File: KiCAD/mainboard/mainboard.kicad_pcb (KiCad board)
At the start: 2 copper layers, 38 parts, among them IC1 DLPC1438ZEZ, IC2 DLPA2005ERSLT, IC3 SN74AUP1G06DCKR, IC4 SN74AUP1G07DCKR, IC5 SN74AUP1G07DCKR, J1 AXT550124, J10 Conn_01x05_Pin, J30 Conn_01x08_Pin

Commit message: layout, was able to fanout all not power signals without vias inside BGA, will only need normal vias size 0.3mm diameter for GND and power planes, plan is to have DMD signals on their own layer
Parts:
- added C1: 100 uF, tp_library:CAP_EEEFT1V101AP, F.Cu at (257.5, 119.2)
- added C109: 10uF, Capacitor_SMD:C_0603_1608Metric_Pad1.08x0.95mm_HandSolder, F.Cu at (264.4, 134.8)
- added C110: 4.7uF, Capacitor_SMD:C_0603_1608Metric_Pad1.08x0.95mm_HandSolder, F.Cu at (264.4, 137.3)
- added C168: 22uF, Capacitor_SMD:C_0603_1608Metric, F.Cu at (266.5, 173.5)
- added C19: 4.7uF, Capacitor_SMD:C_0603_1608Metric_Pad1.08x0.95mm_HandSolder, F.Cu at (264.4, 122.3)
- added C2: 12pF, Capacitor_SMD:C_0603_1608Metric_Pad1.08x0.95mm_HandSolder, F.Cu at (264.4, 117.2)
- added C21: 22uF, Capacitor_SMD:C_0603_1608Metric, F.Cu at (266.5, 163.5)
- added C211: 22uF, Capacitor_SMD:C_0603_1608Metric, F.Cu at (266.5, 176.0)
- added C212: 22uF, Capacitor_SMD:C_0603_1608Metric, F.Cu at (266.5, 178.5)
- added C22: 22uF, Capacitor_SMD:C_0603_1608Metric, F.Cu at (266.5, 166.0)
- added C24: 100 uF, tp_library:CAP_EEEFT1V101AP, F.Cu at (257.5, 127.3)
- added C25: 4.7uF, Capacitor_SMD:C_0603_1608Metric_Pad1.08x0.95mm_HandSolder, F.Cu at (264.4, 124.8)
- added C26: 100nF, Capacitor_SMD:C_0603_1608Metric_Pad1.08x0.95mm_HandSolder, F.Cu at (264.4, 127.3)
- added C3: 12pF, Capacitor_SMD:C_0603_1608Metric_Pad1.08x0.95mm_HandSolder, F.Cu at (264.4, 119.8)
- added C30: 22uF, Capacitor_SMD:C_0603_1608Metric, F.Cu at (266.5, 168.5)
- added C31: 22uF, Capacitor_SMD:C_0603_1608Metric, F.Cu at (266.5, 171.0)
- added C41: 12pF, Capacitor_SMD:C_0603_1608Metric_Pad1.08x0.95mm_HandSolder, F.Cu at (264.4, 129.8)
- added C51: 100pF, Capacitor_SMD:C_0603_1608Metric_Pad1.08x0.95mm_HandSolder, F.Cu at (264.4, 132.3)
- added C71: 10 uF, Capacitor_SMD:C_0805_2012Metric_Pad1.18x1.45mm_HandSolder, F.Cu at (269.0, 117.5)
- added C72: 10 uF, Capacitor_SMD:C_0805_2012Metric_Pad1.18x1.45mm_HandSolder, F.Cu at (269.0, 120.5)
- added C73: 10 uF, Capacitor_SMD:C_0805_2012Metric_Pad1.18x1.45mm_HandSolder, F.Cu at (269.0, 123.5)
- added C74: 10 uF, Capacitor_SMD:C_0805_2012Metric_Pad1.18x1.45mm_HandSolder, F.Cu at (269.0, 126.5)
- added C82: 100 uF, tp_library:CAP_EEEFT1V101AP, F.Cu at (257.5, 135.5)
- added C96: 100 uF, tp_library:CAP_EEEFT1V101AP, F.Cu at (257.5, 143.7)
- added D10: B560C, tp_library:SMC_DIO, F.Cu at (279.9, 132.5)
- added D12: LED, LED_SMD:LED_0603_1608Metric_Pad1.05x0.95mm_HandSolder, F.Cu at (280.1, 116.5)
- added D7: SML-LX1206SIC-TR, tp_library:LED_SML-LX1206SIC-TR_LUM-M, F.Cu at (219.0, 144.3)
- added F2: 1500mA, tp_library:BLM15P_FBD-M, F.Cu at (177.1, 63.8)
- added F3: 1500mA, tp_library:BLM15P_FBD-M, F.Cu at (177.1, 66.6)
- added IC14: SN74AUP1G06DCKR, tp_library:SOT65P210X110-5N, F.Cu at (230.5, 121.2)
- added IC6: SN74AUP1G06DCKR, tp_library:SOT65P210X110-5N, F.Cu at (230.5, 117.5)
- added J10: Conn_01x05_Pin, Connector_PinHeader_2.54mm:PinHeader_1x05_P2.54mm_Vertical, F.Cu at (222.3, 130.0)
- added J100: AHDF15A-KG-TAXB, tp_library:AHDF15AKGTAXB, F.Cu at (218.9, 166.8)
- added J14: Conn_01x04_Pin, Connector_PinHeader_2.54mm:PinHeader_1x04_P2.54mm_Vertical, F.Cu at (253.0, 164.2)
- added J2: Conn_01x07_Pin, Connector_PinHeader_2.54mm:PinHeader_1x07_P2.54mm_Vertical, F.Cu at (213.1, 130.0)
- added J29: Conn_01x04_Pin, Connector_PinHeader_2.54mm:PinHeader_1x04_P2.54mm_Vertical, F.Cu at (204.3, 140.4)
- added J3: Conn_02x05_Odd_Even, Connector_PinHeader_2.54mm:PinHeader_2x05_P2.54mm_Vertical, F.Cu at (226.9, 130.0)
- added J31: Conn_01x08_Pin, Connector_PinHeader_2.54mm:PinHeader_1x08_P2.54mm_Vertical, F.Cu at (248.0, 25.9)
- added J4: Conn_01x05_Pin, Connector_PinHeader_2.54mm:PinHeader_1x05_P2.54mm_Vertical, F.Cu at (217.7, 130.0)
- added L12: LQM2HPN2R2MG0L, tp_library:IND_LQM2HPN2R2MG0L_MUR, F.Cu at (274.7, 144.5)
- added R100: 22.1k, Resistor_SMD:R_0402_1005Metric, F.Cu at (272.9, 123.0)
- added R117: 3.3k, tp_library:RES_ERJP06_PAN, F.Cu at (280.6, 120.0)
- added R155: 10k, tp_library:STA_RMCF0805_STP, F.Cu at (217.2, 120.2)
- added R156: 0, tp_library:RES_R-070RL_VIS, F.Cu at (208.7, 129.2)
- added R157: 0, tp_library:RES_R-070RL_VIS, F.Cu at (208.7, 132.2)
- added R158: 10k, tp_library:STA_RMCF0805_STP, F.Cu at (217.2, 123.2)
- added R16: 0, tp_library:RES_R-070RL_VIS, F.Cu at (197.5, 69.1)
- added R163: 10k, tp_library:STA_RMCF0805_STP, F.Cu at (217.2, 126.2)
- added R164: 10k, tp_library:STA_RMCF0805_STP, F.Cu at (221.5, 117.2)
- added R165: 10k, tp_library:STA_RMCF0805_STP, F.Cu at (221.5, 120.2)
- added R166: 10k, tp_library:STA_RMCF0805_STP, F.Cu at (221.5, 123.2)
- added R168: 100k, tp_library:RES_RMCF0805_STP, F.Cu at (225.9, 123.2)
- added R17: 100k, tp_library:RES_RMCF0805_STP, F.Cu at (232.0, 97.5)
- added R170: 10k, tp_library:STA_RMCF0805_STP, F.Cu at (221.5, 126.2)
- added R171: 0, tp_library:RES_R-070RL_VIS, F.Cu at (208.7, 135.2)
- added R174: 100k, tp_library:RES_RMCF0805_STP, F.Cu at (225.9, 126.2)
- added R19: 100k, tp_library:RES_RMCF0805_STP, F.Cu at (225.9, 120.2)
- added R212: 78.7k, Resistor_SMD:R_0402_1005Metric, F.Cu at (272.9, 124.9)
- added R213: 360k, Resistor_SMD:R_0402_1005Metric, F.Cu at (272.9, 126.9)
- added R3: 78.7k, Resistor_SMD:R_0402_1005Metric, F.Cu at (281.5, 123.0)
- added R42: 7.87k, tp_library:RES_RM10_CCE, F.Cu at (208.7, 123.2)
- added R5: 100, tp_library:RES_CRCW_0805, F.Cu at (217.5, 147.7)
- added R52: 7.87k, tp_library:RES_RM10_CCE, F.Cu at (208.7, 126.2)
- added R53: 3.3k, tp_library:RES_ERJP06_PAN, F.Cu at (212.9, 117.2)
- added R54: 3.3k, tp_library:RES_ERJP06_PAN, F.Cu at (212.9, 120.2)
- added R55: 3.3k, tp_library:RES_ERJP06_PAN, F.Cu at (212.6, 123.6)
- added R7: 100, tp_library:RES_CRCW_0805, F.Cu at (217.5, 150.8)
- added R73: 3.3k, tp_library:RES_ERJP06_PAN, F.Cu at (212.9, 126.2)
- added R8: 0, tp_library:RES_R-070RL_VIS, F.Cu at (208.7, 117.2)
- added R84: 10k, tp_library:STA_RMCF0805_STP, F.Cu at (259.6, 166.5)
- added R92: 10k, tp_library:STA_RMCF0805_STP, F.Cu at (217.2, 117.2)
- added R95: 22.1k, Resistor_SMD:R_0402_1005Metric, F.Cu at (282.0, 126.0)
- added R99: 22.1k, Resistor_SMD:R_0402_1005Metric, F.Cu at (272.9, 121.0)
- added TP12: TestPoint, TestPoint:TestPoint_Pad_D1.5mm, F.Cu at (233.5, 133.0)
- added TP20: TestPoint, TestPoint:TestPoint_Pad_D1.5mm, F.Cu at (233.5, 136.6)
- added TP21: TestPoint, TestPoint:TestPoint_Pad_D1.5mm, F.Cu at (233.5, 140.1)
- added TP7: TestPoint, TestPoint:TestPoint_Pad_D1.5mm, F.Cu at (233.5, 129.5)
- added U12: ECS-2520MV-xxx-xx, Oscillator:Oscillator_SMD_ECS_2520MV-xxx-xx-4Pin_2.5x2.0mm, F.Cu at (196.8, 58.6)
- added U13: MX25L3233FM2, Package_SO:SOIC-8_5.3x5.3mm_P1.27mm, F.Cu at (229.7, 146.0)
- added U22: TXS0102DCU, Package_SO:VSSOP-8_2.3x2mm_P0.5mm, F.Cu at (232.0, 102.5)
- added U26: TPS54340DDA, Package_SO:TI_SO-PowerPAD-8_ThermalVias, F.Cu at (270.9, 139.3)
- added U37: TXS0102DCU, Package_SO:VSSOP-8_2.3x2mm_P0.5mm, F.Cu at (232.0, 108.0)
- added U39: TPS62260DDCT, tp_library:DDC5, F.Cu at (269.4, 144.9)
- added U7: SN74AUP1G06DCKR, tp_library:SOT65P210X110-5N, F.Cu at (230.5, 124.9)
- C169: renamed from C22; value 22u -> 22uF
- R15, R197: footprint Resistor_SMD:R_0402_1005Metric -> tp_library:STA_RMCF0805_STP
- R176, R177, R178, R179: footprint Resistor_SMD:R_0402_1005Metric -> tp_library:RES_RMCF0805_STP
- moved REF** 208.1 mm to (59.5, 229.0)
- moved REF** 208.1 mm to (49.0, 234.5)
- moved REF** 208.1 mm to (24.0, 237.5)
- moved REF** 208.1 mm to (85.5, 235.5)
- moved REF** 208.1 mm to (24.5, 229.5)
- moved REF** 208.1 mm to (48.5, 229.0)
- moved REF** 208.1 mm to (69.5, 244.0)
- moved REF** 208.1 mm to (50.0, 239.5)
- moved REF** 208.1 mm to (69.5, 234.5)
- moved REF** 197.9 mm to (35.8, 222.0)
- moved U16 53.3 mm to (206.8, 59.0)
- moved J1 27.3 mm to (94.9, 52.2)
- moved U24 27.3 mm to (149.8, 51.5)
- moved C116 12.7 mm to (138.5, 94.5)
- moved C117 12.7 mm to (138.5, 96.5)
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- renumbered IC1 to U16, IC2 to U24
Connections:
- net GPIO_12 renamed /DLPC1438_Interface/GPIO_12
- net GPIO_15 renamed /DLPC1438_Interface/GPIO_15
- net GPIO_16 renamed /DLPC1438_Interface/GPIO_16
- net GPIO_17 renamed /DLPC1438_Interface/GPIO_17
- net GPIO_18 renamed /DLPC1438_Interface/GPIO_18
- net GPIO_19 renamed /DLPC1438_Interface/GPIO_19
- net GPIO_4 renamed /DLPC1438_Interface/GPIO_4
- net GPIO_5 renamed /DLPC1438_Interface/GPIO_5
- C116 pad 1: P1P8V_DLPC -> GND
- C116 pad 2: GND -> P1P8V_DLPC
- C122 pad 1: /DMD_Interface/VOFS -> GND
- C122 pad 2: GND -> /DMD_Interface/VOFS
- C123 pad 1: /DMD_Interface/VBIAS -> GND
- C123 pad 2: GND -> /DMD_Interface/VBIAS
- C124 pad 1: /DMD_Interface/VRST -> GND
- C124 pad 2: GND -> /DMD_Interface/VRST
- C13 pad 1: /DMD_Interface/VRST -> GND
- C13 pad 2: GND -> /DMD_Interface/VRST
- C14 pad 1: /DMD_Interface/VBIAS -> GND
- C14 pad 2: GND -> /DMD_Interface/VBIAS
- C15 pad 1: /DMD_Interface/VOFS -> GND
- C15 pad 2: GND -> /DMD_Interface/VOFS
- C169 pad 1: unconnected-(C22-Pad1) -> P5V
- C169 pad 2: unconnected-(C22-Pad2) -> GND
- R15 pad 1: P3V3V -> /DMD_Interface/SYS_RDY
- R15 pad 2: /DMD_Interface/SYS_RDY -> P3V3V
- R176 pad 1: SPI1_CLK -> /DLPC1438_Interface/SPI1_CLK
- R177 pad 1: SPI1_CSZ0 -> P1P8V_DLPC
- R177 pad 2: P1P8V_DLPC -> /DLPC1438_Interface/GPIO_3
- R178 pad 1: GND -> /DLPC1438_Interface/SPI1_MOSI
- R178 pad 2: SPI1_MOSI -> GND
- R179 pad 1: GND -> /DLPC1438_Interface/SPI1_MISO
- R179 pad 2: SPI1_MISO -> GND
- R197 pad 1: P3V3V -> /DMD_Interface/PRINT_ACTIVE
- R197 pad 2: /DMD_Interface/PRINT_ACTIVE -> P3V3V
- U16 pad A12: unconnected-(IC1-CMP_OUT-PadA12) -> /DLPC1438_Interface/CMP_OUT
- U16 pad A13: unconnected-(IC1-SPI0_CLK-PadA13) -> /DLPC1438_Interface/DLPC_SPICLK
- U16 pad A14: unconnected-(IC1-SPI0_CSZ0-PadA14) -> /DLPC1438_Interface/DLPC_SPICSZ0
- U16 pad B12: unconnected-(IC1-SPI0_DIN-PadB12) -> /DLPC1438_Interface/SPI0_MISO
- U16 pad B13: unconnected-(IC1-SPI0_DOUT-PadB13) -> /DLPC1438_Interface/DLPC_SPIDOUT
- U16 pad B14: unconnected-(IC1-LED_SEL_1-PadB14) -> /DLPC1438_Interface/DLPC_LED_SEL_1
- U16 pad B15: unconnected-(IC1-LED_SEL_0-PadB15) -> /DLPC1438_Interface/DLPC_LED_SEL_0
- U16 pad C10: unconnected-(IC1-HWTEST_E_N-PadC10) -> GND
- U16 pad C11: unconnected-(IC1-RESETZ-PadC11) -> /DLPC1438_Interface/RESETZ
- U16 pad C13: unconnected-(IC1-PARKZ-PadC13) -> /DLPC1438_Interface/INTZ
- U16 pad C14: SPI1_MISO -> /DLPC1438_Interface/SPI1_MISO
- U16 pad C3: unconnected-(IC1-VDDLP12-PadC3) -> P1P1V
- U16 pad C4: unconnected-(IC1-VSS_1-PadC4) -> GND
- U16 pad C5: unconnected-(IC1-VDD_1-PadC5) -> P1P1V
- U16 pad C6: unconnected-(IC1-VSS_2-PadC6) -> GND
- U16 pad C7: unconnected-(IC1-VCC_1-PadC7) -> /DLPC1438_Interface/VCC
- U16 pad C8: unconnected-(IC1-VSS_3-PadC8) -> GND
- U16 pad C9: unconnected-(IC1-VCC_2-PadC9) -> /DLPC1438_Interface/VCC
- U16 pad D10: unconnected-(IC1-VSS_6-PadD10) -> GND
- U16 pad D11: unconnected-(IC1-VCC_FLSH-PadD11) -> P3P3V_SB
- U16 pad D12: unconnected-(IC1-VDD_6-PadD12) -> P1P1V
- U16 pad D13: unconnected-(IC1-VDD_7-PadD13) -> P1P1V
- U16 pad D3: unconnected-(IC1-VDD_2-PadD3) -> P1P1V
- U16 pad D4: unconnected-(IC1-VCC_3-PadD4) -> P1P8V_DLPC
- U16 pad D5: unconnected-(IC1-VDD_3-PadD5) -> P1P1V
- U16 pad D6: unconnected-(IC1-VSS_4-PadD6) -> GND
- U16 pad D7: unconnected-(IC1-VDD_4-PadD7) -> P1P1V
- U16 pad D8: unconnected-(IC1-VSS_5-PadD8) -> GND
- U16 pad D9: unconnected-(IC1-VDD_5-PadD9) -> P1P1V
- U16 pad E12: unconnected-(IC1-VCC_4-PadE12) -> P1P8V_DLPC
- U16 pad E13: unconnected-(IC1-VSS_8-PadE13) -> GND
- U16 pad E3: unconnected-(IC1-VDD_8-PadE3) -> P1P1V
- U16 pad E4: unconnected-(IC1-VSS_7-PadE4) -> GND
- U16 pad F10: unconnected-(IC1-VSS_14-PadF10) -> Net-(U16-VSS_10)
- U16 pad F12: unconnected-(IC1-VCC_5-PadF12) -> P1P8V_DLPC
- U16 pad F13: unconnected-(IC1-VDD_9-PadF13) -> P1P1V
- U16 pad F4: unconnected-(IC1-VSS_9-PadF4) -> GND
- U16 pad F6: unconnected-(IC1-VSS_10-PadF6) -> Net-(U16-VSS_10)
- U16 pad F7: unconnected-(IC1-VSS_11-PadF7) -> Net-(U16-VSS_10)
- U16 pad F8: unconnected-(IC1-VSS_12-PadF8) -> Net-(U16-VSS_10)
- U16 pad F9: unconnected-(IC1-VSS_13-PadF9) -> Net-(U16-VSS_10)
- U16 pad G10: unconnected-(IC1-VSS_20-PadG10) -> GND
- U16 pad G12: unconnected-(IC1-VSS_21-PadG12) -> GND
- U16 pad G13: unconnected-(IC1-VSS_22-PadG13) -> GND
- U16 pad G14: /DLPC1438_Interface/PROJ_ON -> /DLPA2005_Interface/PROJ_ON
- U16 pad G3: unconnected-(IC1-VSS_PLLM-PadG3) -> /DLPC1438_Interface/VSS_PLL
- U16 pad G4: unconnected-(IC1-VSS_15-PadG4) -> GND
- U16 pad G6: unconnected-(IC1-VSS_16-PadG6) -> GND
- U16 pad G7: unconnected-(IC1-VSS_17-PadG7) -> GND
- U16 pad G8: unconnected-(IC1-VSS_18-PadG8) -> GND
- U16 pad G9: unconnected-(IC1-VSS_19-PadG9) -> GND
- U16 pad H1: unconnected-(IC1-PLL_REFCL_K_I-PadH1) -> /DLPC1438_Interface/OSC_OUT
- U16 pad H10: unconnected-(IC1-VSS_28-PadH10) -> GND
- U16 pad H12: unconnected-(IC1-VSS_29-PadH12) -> GND
- U16 pad H13: unconnected-(IC1-VDD_10-PadH13) -> P1P1V
- U16 pad H14: /DLPC1438_Interface/RC_CHARGE -> /DLPA2005_Interface/RC_CHARGE
- U16 pad H2: unconnected-(IC1-VDD_PLLM-PadH2) -> /DLPC1438_Interface/VDD_PLL
- U16 pad H3: unconnected-(IC1-VSS_PLLD-PadH3) -> /DLPC1438_Interface/VSS_PLL
- U16 pad H4: unconnected-(IC1-VSS_23-PadH4) -> GND
- U16 pad H6: unconnected-(IC1-VSS_24-PadH6) -> GND
- U16 pad H7: unconnected-(IC1-VSS_25-PadH7) -> GND
- U16 pad H8: unconnected-(IC1-VSS_26-PadH8) -> GND
- U16 pad H9: unconnected-(IC1-VSS_27-PadH9) -> GND
- U16 pad J1: unconnected-(IC1-PLL_REFCL_K_O-PadJ1) -> /DLPC1438_Interface/DLPC_PLLO
- U16 pad J10: unconnected-(IC1-VSS_35-PadJ10) -> GND
- U16 pad J12: unconnected-(IC1-VDD_12-PadJ12) -> P1P1V
- U16 pad J13: unconnected-(IC1-VSS_36-PadJ13) -> GND
- U16 pad J2: unconnected-(IC1-VDD_PLLD-PadJ2) -> /DLPC1438_Interface/VDD_PLL
- U16 pad J3: unconnected-(IC1-VSS_30-PadJ3) -> GND
- U16 pad J4: unconnected-(IC1-VDD_11-PadJ4) -> P1P1V
- U16 pad J6: unconnected-(IC1-VSS_31-PadJ6) -> GND
- U16 pad J7: unconnected-(IC1-VSS_32-PadJ7) -> GND
- U16 pad J8: unconnected-(IC1-VSS_33-PadJ8) -> GND
- U16 pad J9: unconnected-(IC1-VSS_34-PadJ9) -> GND
- U16 pad K1: unconnected-(IC1-PDATA_1-PadK1) -> /DLPC1438_Interface/PDATA1
- U16 pad K10: unconnected-(IC1-VSS_42-PadK10) -> GND
- U16 pad K12: unconnected-(IC1-VSS_43-PadK12) -> GND
- U16 pad K13: unconnected-(IC1-VCC_6-PadK13) -> P1P8V_DLPC
- U16 pad K2: unconnected-(IC1-PDATA_0-PadK2) -> /DLPC1438_Interface/PDATA0
- U16 pad K3: unconnected-(IC1-VDD_13-PadK3) -> P1P1V
- U16 pad K4: unconnected-(IC1-VSS_37-PadK4) -> GND
- U16 pad K6: unconnected-(IC1-VSS_38-PadK6) -> GND
- U16 pad K7: unconnected-(IC1-VSS_39-PadK7) -> GND
- U16 pad K8: unconnected-(IC1-VSS_40-PadK8) -> GND
- U16 pad K9: unconnected-(IC1-VSS_41-PadK9) -> GND
- U16 pad L1: unconnected-(IC1-PDATA_3-PadL1) -> /DLPC1438_Interface/PDATA3
- U16 pad L12: unconnected-(IC1-VDD_15-PadL12) -> P1P1V
- U16 pad L13: unconnected-(IC1-VDD_16-PadL13) -> P1P1V
- U16 pad L2: unconnected-(IC1-PDATA_2-PadL2) -> /DLPC1438_Interface/PDATA2
- U16 pad L3: unconnected-(IC1-VSS_44-PadL3) -> GND
- U16 pad L4: unconnected-(IC1-VDD_14-PadL4) -> P1P1V
- U16 pad M1: unconnected-(IC1-PDATA_5-PadM1) -> /DLPC1438_Interface/PDATA5
- U16 pad M10: unconnected-(IC1-VDD_19-PadM10) -> P1P1V
- U16 pad M11: unconnected-(IC1-VCC_7-PadM11) -> P1P8V_DLPC
- U16 pad M12: unconnected-(IC1-VSS_48-PadM12) -> GND
- U16 pad M13: unconnected-(IC1-JTAGTMS1-PadM13) -> /DLPC1438_Interface/JTAG_TMS
- U16 pad M2: unconnected-(IC1-PDATA_4-PadM2) -> /DLPC1438_Interface/PDATA4
- U16 pad M3: unconnected-(IC1-VCC_INTF_1-PadM3) -> P1P8V_DLPC
- U16 pad M4: unconnected-(IC1-VSS_45-PadM4) -> GND
- U16 pad M5: unconnected-(IC1-VSS_46-PadM5) -> GND
- U16 pad M6: unconnected-(IC1-VDD_17-PadM6) -> P1P1V
- U16 pad M7: unconnected-(IC1-VCC_INTF_2-PadM7) -> P1P8V_DLPC
- U16 pad M8: unconnected-(IC1-VSS_47-PadM8) -> GND
- U16 pad M9: unconnected-(IC1-VDD_18-PadM9) -> P1P1V
- U16 pad N1: unconnected-(IC1-PDATA_7-PadN1) -> /DLPC1438_Interface/PDATA7
- U16 pad N10: unconnected-(IC1-IIC0_SCL-PadN10) -> /DLPC1438_Interface/IIC0_SCL
- U16 pad N13: unconnected-(IC1-JTAGTDO1-PadN13) -> /DLPC1438_Interface/JTAG_TDO
- U16 pad N14: unconnected-(IC1-TSTPT_6-PadN14) -> /DLPC1438_Interface/TSTPT_6
- U16 pad N15: unconnected-(IC1-TSTPT_7-PadN15) -> /DLPC1438_Interface/TSTPT_7
- U16 pad N2: unconnected-(IC1-PDATA_6-PadN2) -> /DLPC1438_Interface/PDATA6
- U16 pad N3: unconnected-(IC1-VCC_INTF_3-PadN3) -> P1P8V_DLPC
- U16 pad N4: unconnected-(IC1-PDM_CVS__TE-PadN4) -> /DLPC1438_Interface/PDM_CVS_TE
- U16 pad N5: unconnected-(IC1-HSYNC_CS-PadN5) -> /DLPC1438_Interface/HSYNC
- U16 pad N6: unconnected-(IC1-3DR-PadN6) -> /DLPC1438_Interface/DLPC_3DR
- U16 pad N7: unconnected-(IC1-VCC_INTF_4-PadN7) -> P1P8V_DLPC
- U16 pad N8: unconnected-(IC1-HOST_IRQ-PadN8) -> /DLPC1438_Interface/DLPC_HOST_IRQ
- U16 pad N9: unconnected-(IC1-IIC0_SDA-PadN9) -> /DLPC1438_Interface/IIC0_SDA
- U16 pad P1: unconnected-(IC1-VSYNC_WE-PadP1) -> /DLPC1438_Interface/VSYNC
- U16 pad P10: unconnected-(IC1-PDATA_23-PadP10) -> GND
- U16 pad P11: unconnected-(IC1-JTAGTRSTZ-PadP11) -> /DLPC1438_Interface/JTAG_TRSTZ
- U16 pad P12: unconnected-(IC1-JTAGTCK-PadP12) -> /DLPC1438_Interface/JTAG_TCK
- U16 pad P13: unconnected-(IC1-JTAGTDI-PadP13) -> /DLPC1438_Interface/JTAG_TDI
- U16 pad P14: unconnected-(IC1-TSTPT_4-PadP14) -> /DLPC1438_Interface/TSTPT_4
- U16 pad P15: unconnected-(IC1-TSTPT_5-PadP15) -> /DLPC1438_Interface/TSTPT_5
- U16 pad P2: unconnected-(IC1-DATEN_CM_D-PadP2) -> /DLPC1438_Interface/DATEN_CM_D
- U16 pad P3: unconnected-(IC1-PCLK-PadP3) -> /DLPC1438_Interface/PCLK
- U16 pad P4: unconnected-(IC1-PDATA_11-PadP4) -> GND
- U16 pad P5: unconnected-(IC1-PDATA_13-PadP5) -> GND
- U16 pad P6: unconnected-(IC1-PDATA_15-PadP6) -> GND
- U16 pad P7: unconnected-(IC1-PDATA_17-PadP7) -> GND
- U16 pad P8: unconnected-(IC1-PDATA_19-PadP8) -> GND
- U16 pad P9: unconnected-(IC1-PDATA_21-PadP9) -> GND
- U16 pad R1: unconnected-(IC1-PDATA_8-PadR1) -> GND
- U16 pad R10: unconnected-(IC1-IIC1_SDA-PadR10) -> /DLPC1438_Interface/IIC1_SCL
- U16 pad R11: unconnected-(IC1-IIC1_SCL-PadR11) -> /DLPC1438_Interface/IIC1_SDA
- U16 pad R12: unconnected-(IC1-TSTPT_0-PadR12) -> /DLPC1438_Interface/TSTPT_0
- U16 pad R13: unconnected-(IC1-TSTPT_1-PadR13) -> /DLPC1438_Interface/TSTPT_1
- U16 pad R14: unconnected-(IC1-TSTPT_2-PadR14) -> /DLPC1438_Interface/TSTPT_2
- U16 pad R15: unconnected-(IC1-TSTPT_3-PadR15) -> /DLPC1438_Interface/TSTPT_3
- U16 pad R2: unconnected-(IC1-PDATA_9-PadR2) -> GND
- U16 pad R3: unconnected-(IC1-PDATA_10-PadR3) -> GND
- U16 pad R4: unconnected-(IC1-PDATA_12-PadR4) -> GND
- U16 pad R5: unconnected-(IC1-PDATA_14-PadR5) -> GND
- U16 pad R6: unconnected-(IC1-PDATA_16-PadR6) -> GND
- U16 pad R7: unconnected-(IC1-PDATA_18-PadR7) -> GND
- U16 pad R8: unconnected-(IC1-PDATA_20-PadR8) -> GND
- U16 pad R9: unconnected-(IC1-PDATA_22-PadR9) -> GND
- U24 pad 1: unconnected-(IC2-VINL_1-Pad1) -> P5V
- U24 pad 10: unconnected-(IC2-VINR-Pad10) -> P5V
- U24 pad 11: unconnected-(IC2-SWN-Pad11) -> Net-(D18-K)
- U24 pad 12: unconnected-(IC2-PGNDR-Pad12) -> GND
- U24 pad 13: unconnected-(IC2-SWP-Pad13) -> Net-(U24-SWP)
- U24 pad 14: unconnected-(IC2-CNTR_VRST-Pad14) -> VRST
- U24 pad 15: unconnected-(IC2-VBIAS-Pad15) -> VBIAS
- U24 pad 17: unconnected-(IC2-VOFS-Pad17) -> VOFS
- U24 pad 18: unconnected-(IC2-VINA-Pad18) -> P5V
- U24 pad 19: unconnected-(IC2-V2V5-Pad19) -> V2V5
- U24 pad 2: unconnected-(IC2-VINL_2-Pad2) -> P5V
- U24 pad 20: unconnected-(IC2-GND-Pad20) -> GND
- U24 pad 21: unconnected-(IC2-LS_OUT-Pad21) -> Net-(U24-LS_OUT)
- U24 pad 22: unconnected-(IC2-LS_IN-Pad22) -> P1P8V
- U24 pad 23: unconnected-(IC2-PGNDC-Pad23) -> GND
- U24 pad 24: unconnected-(IC2-SWC-Pad24) -> Net-(U24-SWC)
- U24 pad 25: unconnected-(IC2-VINC-Pad25) -> P5V
- U24 pad 26: unconnected-(IC2-PWM_IN-Pad26) -> /DLPA2005_Interface/RC_CHARGE
- U24 pad 27: unconnected-(IC2-PROJ_ON-Pad27) -> /DLPA2005_Interface/PROJ_ON
- U24 pad 28: unconnected-(IC2-CMP_OUT-Pad28) -> /DLPC1438_Interface/CMP_OUT
- U24 pad 29: unconnected-(IC2-VCORE-Pad29) -> P1P1V
- U24 pad 3: unconnected-(IC2-SPI_DIN-Pad3) -> /DLPC1438_Interface/SPI1_MOSI
- U24 pad 30: unconnected-(IC2-SENS2-Pad30) -> Net-(U24-SENS2)
- U24 pad 31: unconnected-(IC2-LED_SEL0-Pad31) -> Net-(U24-LED_SEL0)
- U24 pad 32: unconnected-(IC2-VSPI-Pad32) -> P1P8V_DLPC
- U24 pad 33: unconnected-(IC2-SENS1-Pad33) -> Net-(U24-SENS1)
- U24 pad 34: unconnected-(IC2-LED_SEL1-Pad34) -> /DLPA2005_Interface/LED_SEL_1
- U24 pad 35: unconnected-(IC2-V6V-Pad35) -> V6V
- U24 pad 36: unconnected-(IC2-RLIM_K-Pad36) -> Net-(U24-RLIM)
- U24 pad 38: unconnected-(IC2-SW5-Pad38) -> /DLPA2005_Interface/GRN_CATHODE
- U24 pad 4: /DLPA2005_Interface/RESETZ -> /DLPC1438_Interface/RESETZ
- U24 pad 40: unconnected-(IC2-RLIM-Pad40) -> Net-(U24-RLIM)
- U24 pad 41: unconnected-(IC2-VLED_1-Pad41) -> /DLPA2005_Interface/LED_ANODE
- U24 pad 42: unconnected-(IC2-VLED_2-Pad42) -> /DLPA2005_Interface/LED_ANODE
- U24 pad 43: unconnected-(IC2-L2_1-Pad43) -> Net-(U24-L2_1)
- U24 pad 44: unconnected-(IC2-L2_2-Pad44) -> Net-(U24-L2_1)
- U24 pad 45: unconnected-(IC2-PGNDL_1-Pad45) -> GND
- U24 pad 46: unconnected-(IC2-PGNDL_2-Pad46) -> GND
- U24 pad 47: unconnected-(IC2-L1_1-Pad47) -> Net-(U24-L1_1)
- U24 pad 48: unconnected-(IC2-L1_2-Pad48) -> Net-(U24-L1_1)
- U24 pad 49: unconnected-(IC2-EP-Pad49) -> GND
- U24 pad 5: unconnected-(IC2-AGND1-Pad5) -> GND
- U24 pad 6: unconnected-(IC2-INTZ-Pad6) -> /DLPC1438_Interface/INTZ
- U24 pad 7: unconnected-(IC2-SPI_CLK-Pad7) -> /DLPC1438_Interface/SPI1_CLK
- U24 pad 8: unconnected-(IC2-SPI_CSZ-Pad8) -> /DLPC1438_Interface/SPI1_CSZ0
- U24 pad 9: unconnected-(IC2-SPI_DOUT-Pad9) -> Net-(U24-SPI_DOUT)
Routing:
- net /DLPC1438_Interface/RESETZ: track 0.00 -> 9.64 mm
- net P1P1V: track 0.00 -> 9.31 mm
- net /DLPC1438_Interface/VSS_PLL: track 0.00 -> 6.40 mm
- net P1P8V_DLPC: track 0.00 -> 5.98 mm
- net /DLPC1438_Interface/VDD_PLL: track 0.00 -> 5.42 mm
- net /DLPC1438_Interface/INTZ: track 0.00 -> 4.11 mm
- net /DLPC1438_Interface/DMD_HS_WDATAC_N: track 0.00 -> 3.52 mm
- net /DLPC1438_Interface/SPI0_MISO: track 0.00 -> 3.44 mm
- net /DLPC1438_Interface/JTAG_TMS: track 0.00 -> 3.44 mm
- net /DLPC1438_Interface/JTAG_TDO: track 0.00 -> 3.43 mm
- net /DLPC1438_Interface/DLPC_SPIDOUT: track 0.00 -> 3.42 mm
- net /DLPC1438_Interface/IIC0_SCL: track 0.00 -> 3.35 mm
- net /DLPC1438_Interface/DMD_HS_WDATAB_N: track 0.00 -> 3.35 mm
- net /DLPC1438_Interface/DMD_HS_WDATAA_N: track 0.00 -> 3.28 mm
- net /DLPC1438_Interface/DLPC_LED_SEL_1: track 0.00 -> 3.21 mm
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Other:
- copper layers 2 -> 10

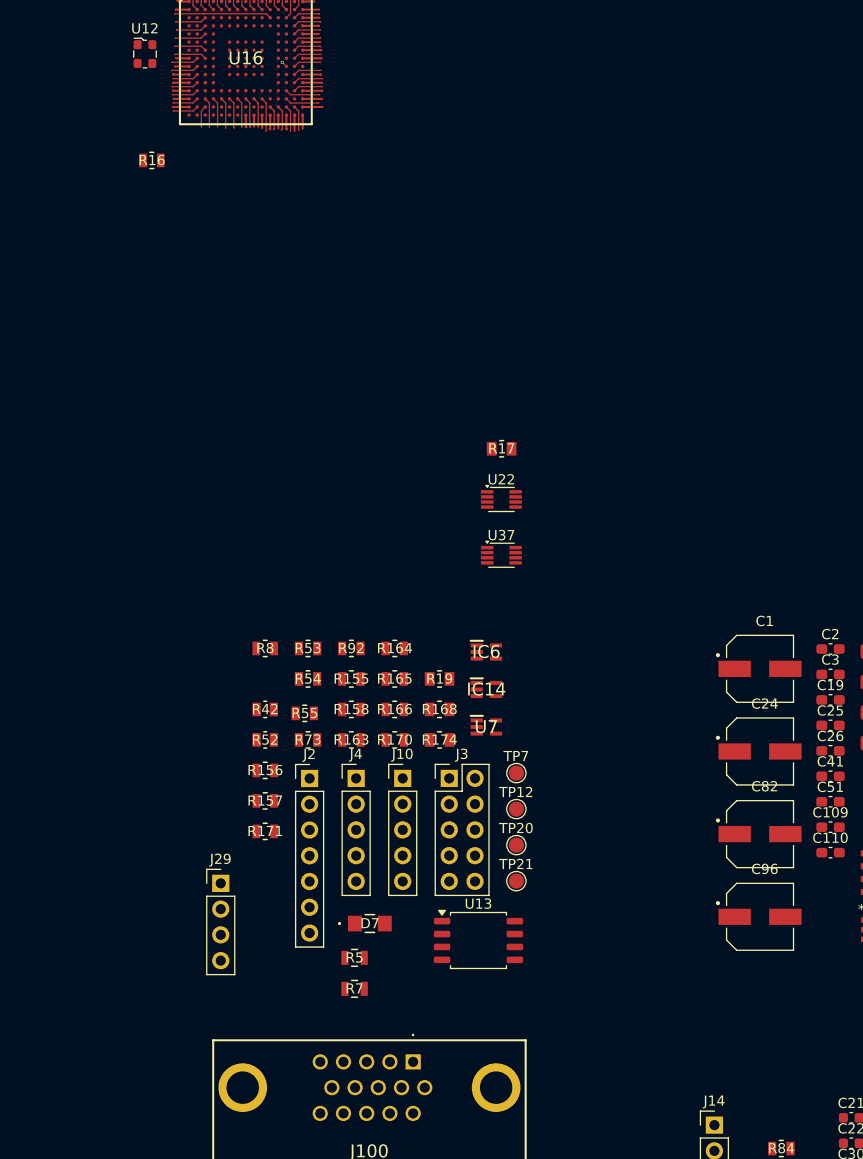
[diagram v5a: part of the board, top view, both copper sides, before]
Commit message: added pours to pcb and fixed DLPC capacitor errors
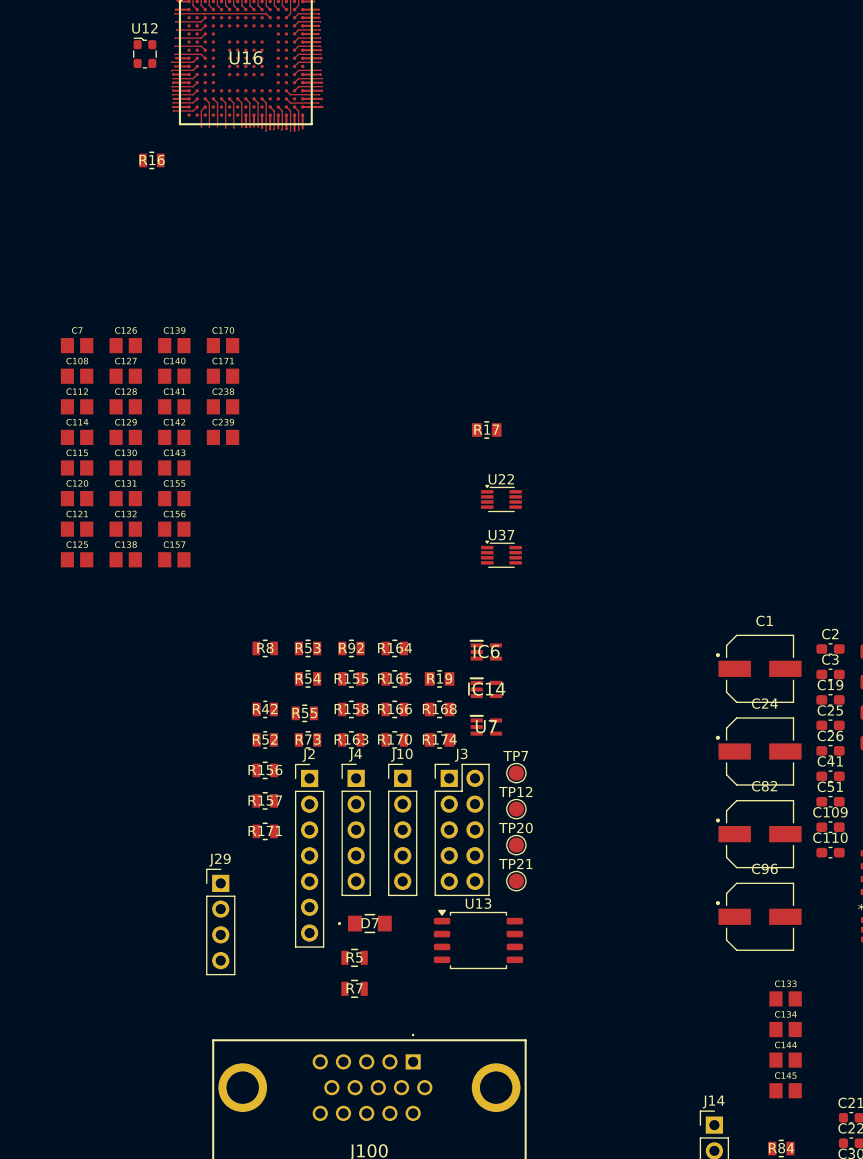
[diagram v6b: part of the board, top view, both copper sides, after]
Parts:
- added C108: 100n, tp_library:CAPC2012X70, F.Cu at (190.2, 90.3)
- added C112: 100n, tp_library:CAPC2012X70, F.Cu at (190.2, 93.4)
- added C114: 100n, tp_library:CAPC2012X70, F.Cu at (190.2, 96.4)
- added C115: 100n, tp_library:CAPC2012X70, F.Cu at (190.2, 99.4)
- added C120: 100n, tp_library:CAPC2012X70, F.Cu at (190.2, 102.4)
- added C121: 100n, tp_library:CAPC2012X70, F.Cu at (190.2, 105.4)
- added C125: 100n, tp_library:CAPC2012X70, F.Cu at (190.2, 108.4)
- added C126: 100n, tp_library:CAPC2012X70, F.Cu at (195.0, 87.3)
- added C127: 100n, tp_library:CAPC2012X70, F.Cu at (195.0, 90.3)
- added C128: 100n, tp_library:CAPC2012X70, F.Cu at (195.0, 93.4)
- added C129: 100n, tp_library:CAPC2012X70, F.Cu at (195.0, 96.4)
- added C130: 100n, tp_library:CAPC2012X70, F.Cu at (195.0, 99.4)
- added C131: 100n, tp_library:CAPC2012X70, F.Cu at (195.0, 102.4)
- added C132: 100n, tp_library:CAPC2012X70, F.Cu at (195.0, 105.4)
- added C133: 100n, tp_library:CAPC2012X70, F.Cu at (260.0, 151.7)
- added C134: 100n, tp_library:CAPC2012X70, F.Cu at (260.0, 154.8)
- added C138: 100n, tp_library:CAPC2012X70, F.Cu at (195.0, 108.4)
- added C139: 100n, tp_library:CAPC2012X70, F.Cu at (199.8, 87.3)
- added C140: 100n, tp_library:CAPC2012X70, F.Cu at (199.8, 90.3)
- added C141: 100n, tp_library:CAPC2012X70, F.Cu at (199.8, 93.4)
- added C142: 100n, tp_library:CAPC2012X70, F.Cu at (199.8, 96.4)
- added C143: 100n, tp_library:CAPC2012X70, F.Cu at (199.8, 99.4)
- added C144: 100n, tp_library:CAPC2012X70, F.Cu at (260.0, 157.8)
- added C145: 100n, tp_library:CAPC2012X70, F.Cu at (260.0, 160.8)
- added C155: 100n, tp_library:CAPC2012X70, F.Cu at (199.8, 102.4)
- added C156: 100n, tp_library:CAPC2012X70, F.Cu at (199.8, 105.4)
- added C157: 100n, tp_library:CAPC2012X70, F.Cu at (199.8, 108.4)
- added C170: 100n, tp_library:CAPC2012X70, F.Cu at (204.5, 87.3)
- added C171: 100n, tp_library:CAPC2012X70, F.Cu at (204.5, 90.3)
- added C238: 100n, tp_library:CAPC2012X70, F.Cu at (204.5, 93.4)
- added C239: 100n, tp_library:CAPC2012X70, F.Cu at (204.5, 96.4)
- added C7: 100n, tp_library:CAPC2012X70, F.Cu at (190.2, 87.3)
- moved R17 2.36 mm to (230.6, 95.7)
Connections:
- U16 pad F10: Net-(U16-VSS_10) -> GND
- U16 pad F6: Net-(U16-VSS_10) -> GND
- U16 pad F7: Net-(U16-VSS_10) -> GND
- U16 pad F8: Net-(U16-VSS_10) -> GND
- U16 pad F9: Net-(U16-VSS_10) -> GND
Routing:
- net GND: track 2.95 -> 2.36 mm, vias 1 -> 0
- added copper zone on In1.Cu, net GND
- added copper zone on In8.Cu, net GND
- added copper zone on In3.Cu, net P1P1V
- added copper zone on In6.Cu, net P1P8V_DLPC
- added copper zone on In5.Cu, net P3P3V

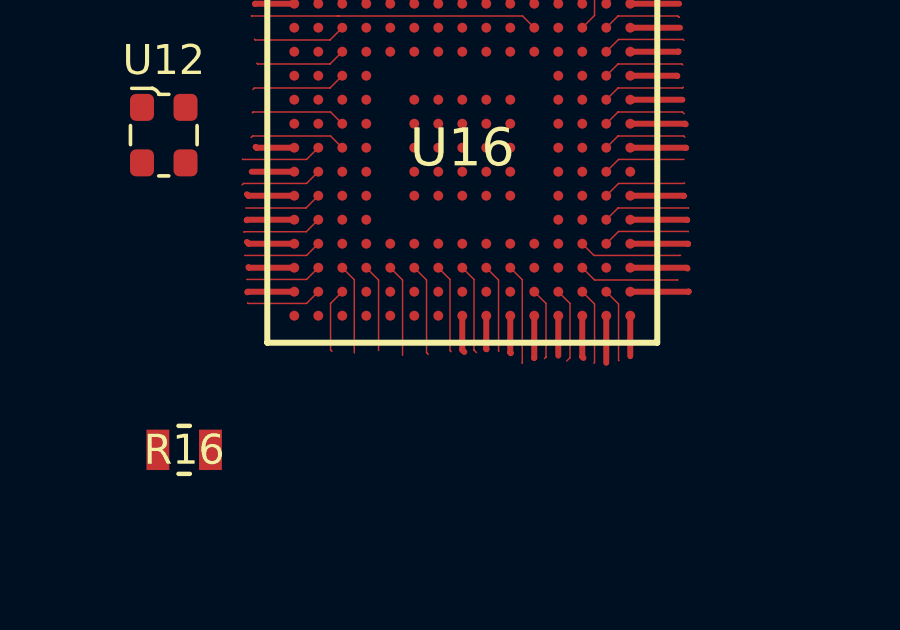
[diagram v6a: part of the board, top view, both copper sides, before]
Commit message: meeting edits to DLPA and DLPC
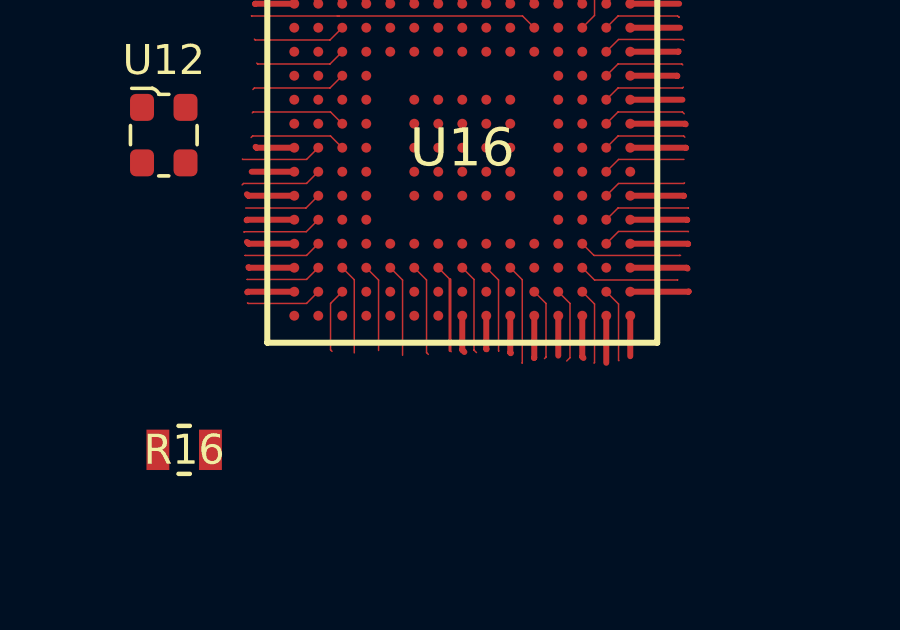
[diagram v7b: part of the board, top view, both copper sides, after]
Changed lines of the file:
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@@
 		(start 206.391 63.391)
 		(end 206.391 65.761)
-		(width 0.05)
+		(width 0.1)
 		(layer "F.Cu")
 		(net 22)

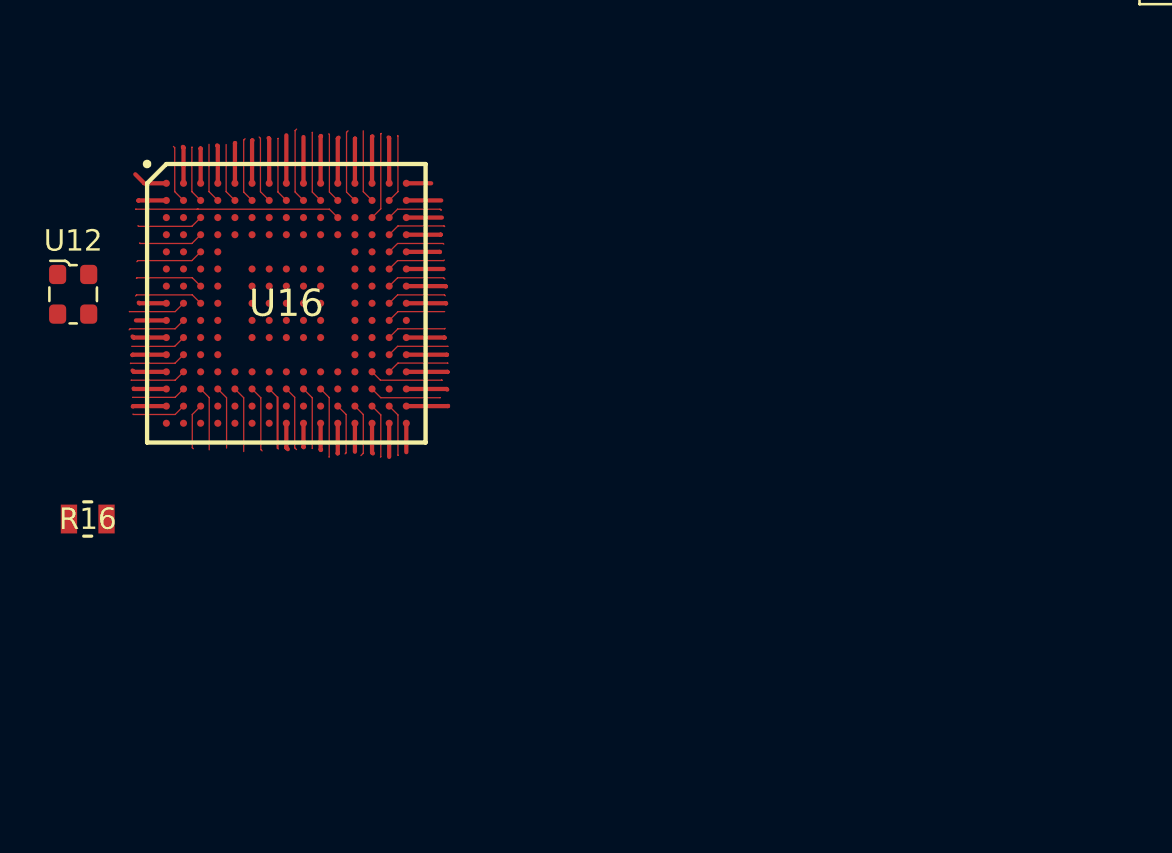
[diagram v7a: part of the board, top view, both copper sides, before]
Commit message: added netclasses and added signals to BGA_Signal, still have to add rest of of signals to other classes but now I'm confused on how BGA traces are smaller but then the same signal could use thicker traces outside the BGA
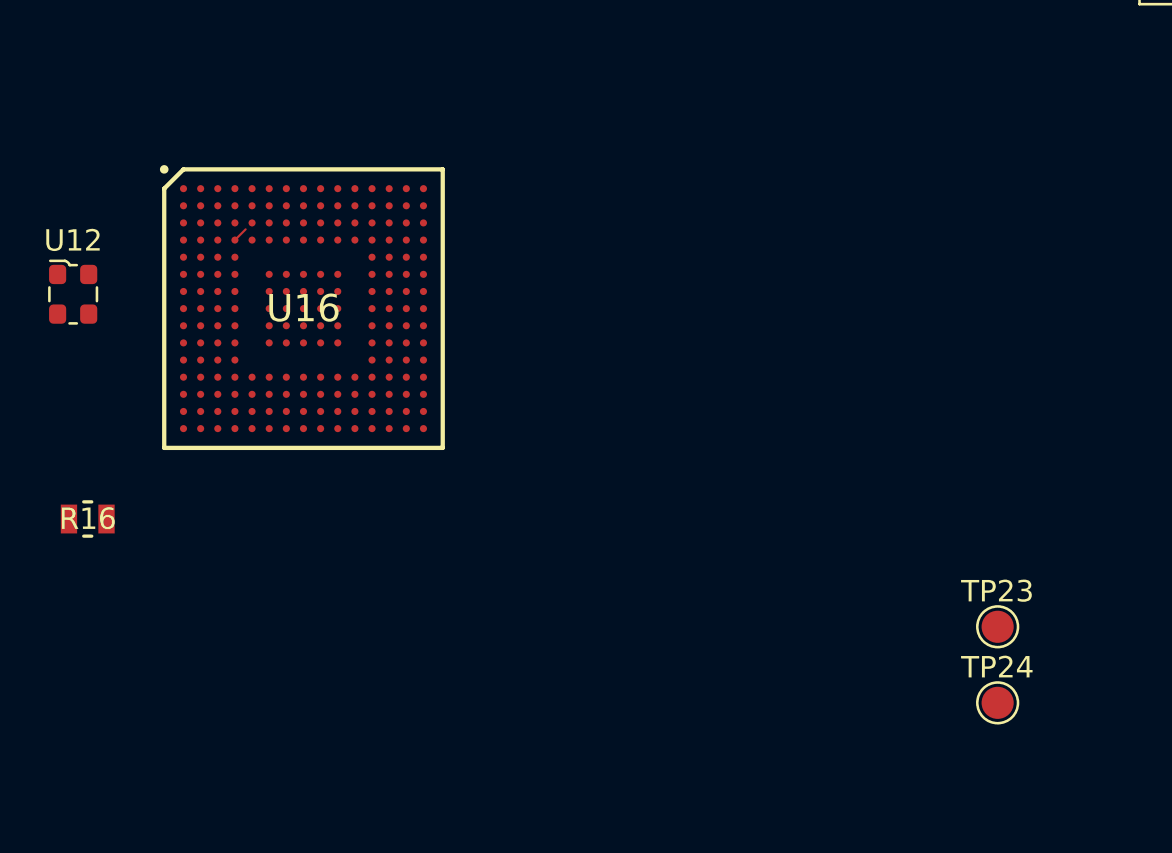
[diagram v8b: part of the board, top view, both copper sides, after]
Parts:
- added TP23: TestPoint, TestPoint:TestPoint_Pad_D1.5mm, F.Cu at (240.0, 74.1)
- added TP24: TestPoint, TestPoint:TestPoint_Pad_D1.5mm, F.Cu at (240.0, 77.7)
- moved U16 0.84 mm to (207.6, 59.2)
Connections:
- net /DLPC1438_Interface/PDM_CVS_TE renamed Net-(U16-PDM_CVS__TE)
- C122 pad 2: /DMD_Interface/VOFS -> VOFS
- C123 pad 2: /DMD_Interface/VBIAS -> VBIAS
- C124 pad 2: /DMD_Interface/VRST -> /DLPA2005_Interface/VRST
- C13 pad 2: /DMD_Interface/VRST -> /DLPA2005_Interface/VRST
- C14 pad 2: /DMD_Interface/VBIAS -> VBIAS
- C15 pad 2: /DMD_Interface/VOFS -> VOFS
- J1 pad 45: /DMD_Interface/VRST -> /DLPA2005_Interface/VRST
- J1 pad 46: /DMD_Interface/VBIAS -> VBIAS
- J1 pad 47: /DMD_Interface/VOFS -> VOFS
- U16 pad C7: /DLPC1438_Interface/VCC -> P1P8V_DLPC
- U16 pad C9: /DLPC1438_Interface/VCC -> P1P8V_DLPC
- U24 pad 14: VRST -> /DLPA2005_Interface/VRST
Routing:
- net /DLPC1438_Interface/RESETZ: track 9.64 -> 0.00 mm
- net P1P1V: track 9.31 -> 0.00 mm
- net /DLPC1438_Interface/VSS_PLL: track 6.40 -> 0.00 mm
- net /DLPC1438_Interface/VDD_PLL: track 5.42 -> 0.00 mm
- net P1P8V_DLPC: track 5.98 -> 0.71 mm
- net /DLPC1438_Interface/INTZ: track 4.11 -> 0.00 mm
- net /DLPC1438_Interface/DMD_HS_WDATAC_N: track 3.52 -> 0.00 mm
- net /DLPC1438_Interface/SPI0_MISO: track 3.44 -> 0.00 mm
- net /DLPC1438_Interface/JTAG_TMS: track 3.44 -> 0.00 mm
- net /DLPC1438_Interface/JTAG_TDO: track 3.43 -> 0.00 mm
- net /DLPC1438_Interface/DLPC_SPIDOUT: track 3.42 -> 0.00 mm
- net /DLPC1438_Interface/IIC0_SCL: track 3.35 -> 0.00 mm
- net /DLPC1438_Interface/DMD_HS_WDATAB_N: track 3.35 -> 0.00 mm
- net /DLPC1438_Interface/DMD_HS_WDATAA_N: track 3.28 -> 0.00 mm
- net /DLPC1438_Interface/DLPC_LED_SEL_1: track 3.21 -> 0.00 mm
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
